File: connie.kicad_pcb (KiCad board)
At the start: 4 copper layers, 105.6 x 58 mm, 143 parts, among them J1 Conn_01x03, J2 Conn_01x02, J3 Conn_01x02, J4 Conn_01x03, J5 Barrel_Jack_Switch, Q1 DTC143Z, Q2 DTC143Z, Q3 DTC143Z, Q4 DTC143Z, SW1 DIP_1188E, SW2 DIP_1188E, SW3 DIP_1188E, SW4 DIP_1188E, SW5 DIP_1188E, U1 emmc_bga153, U2 ESP32_WROVER, U3 ES8388, U4 CS8676E, U5 74LVC1G02, U6 MAX803, U7 MAX803, U8 74LVC1G02, U9 TPS562200

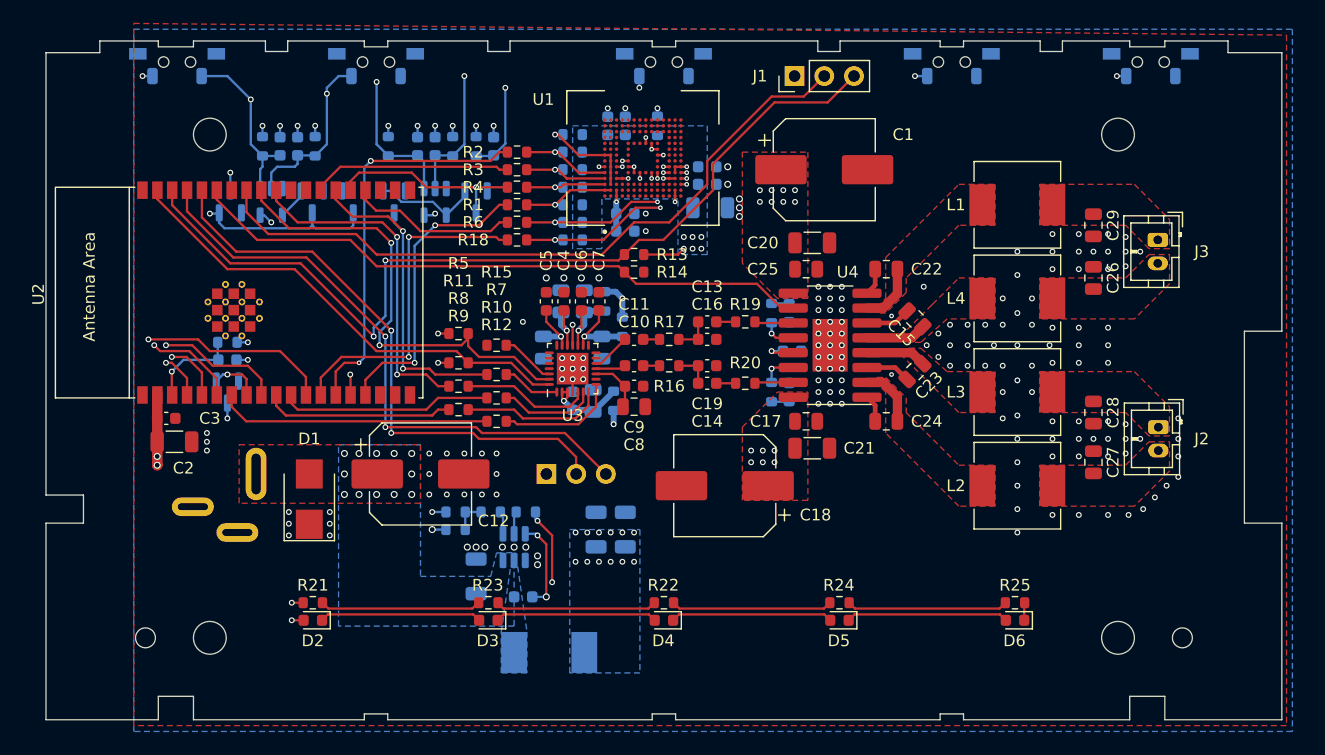
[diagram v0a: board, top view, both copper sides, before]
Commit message: add c3 module
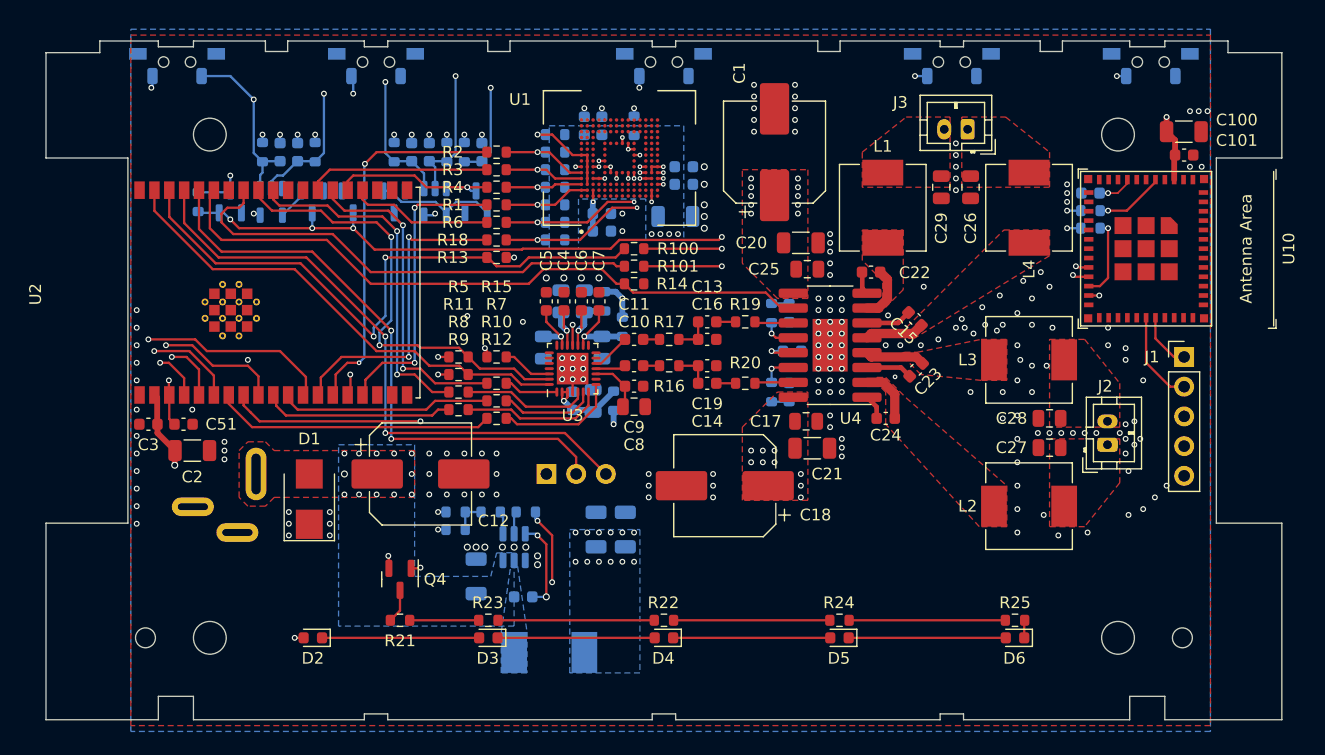
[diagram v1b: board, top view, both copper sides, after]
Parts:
- added C100: 22u, Capacitor_SMD:C_1206_3216Metric, F.Cu at (232.2, 31.8)
- added C101: 0.1u, Capacitor_SMD:C_0603_1608Metric, F.Cu at (232.2, 33.8)
- added C102: 0.1u, Capacitor_SMD:C_0603_1608Metric, B.Cu at (224.2, 37.0)
- added R100: 1k, Resistor_SMD:R_0603_1608Metric, F.Cu at (185.2, 41.8)
- added R101: 1k, Resistor_SMD:R_0603_1608Metric, F.Cu at (185.2, 43.2)
- added R103: 10k, Resistor_SMD:R_0603_1608Metric, B.Cu at (224.2, 38.5)
- added R104: 10k, Resistor_SMD:R_0603_1608Metric, B.Cu at (224.2, 40.0)
- added U10: ESP32-C3-mini-1, Espressif:ESP32-C3-MINI-1, F.Cu at (229.0, 41.8)
- C15, C22, C23, C24: footprint Capacitor_SMD:C_0805_2012Metric -> Capacitor_SMD:C_0603_1608Metric
- C51, Q4: moved to F.Cu
- J1: value Conn_01x03 -> Conn_01x05; footprint Connector_PinHeader_2.54mm:PinHeader_1x03_P2.54mm_Vertical -> Connector_PinHeader_2.54mm:PinHeader_1x05_P2.54mm_Vertical
- R26, R27, R28, R31, R32, R33, R42, R43: value R -> 10k
- moved J1 41.0 mm to (232.2, 51.0), turned to 0 degrees
- moved Q4 21.8 mm to (165.2, 70.0)
- moved J3 18.8 mm to (213.8, 31.6), turned to 180 degrees
- moved C29 13.4 mm to (211.5, 36.5)
- moved C26 13.1 mm to (214.0, 36.5), turned to 90 degrees
- moved R44 12.3 mm to (148.0, 37.8), turned to -90 degrees
- moved R13 11.8 mm to (173.5, 42.5)
- moved L1 11.5 mm to (206.5, 38.2), turned to -90 degrees
- moved L4 7.81 mm to (219.0, 38.2), turned to -90 degrees
- moved R21 7.60 mm to (165.2, 73.5)
- moved C51 6.66 mm to (146.8, 56.8)
- moved J2 4.60 mm to (225.7, 58.5), turned to 90 degrees
- moved C1 4.51 mm to (197.2, 33.5), turned to 90 degrees
- moved C27 3.95 mm to (220.8, 58.8), turned to 0 degrees
- moved C28 3.78 mm to (220.8, 56.2), turned to 180 degrees
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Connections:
- C37 pad 1: /MODE -> GND
- C37 pad 2: GND -> /MODE
- J1 pad 1: GND -> /C3_TXD0
- J1 pad 2: /RXD1 -> /C3_RXD0
- J1 pad 3: /TXD1 -> GND
- J2 pad 1: /OUTNR2 -> /OUTPR2
- J2 pad 2: /OUTPR2 -> /OUTNR2
- J3 pad 1: /OUTPL2 -> /OUTNL2
- J3 pad 2: /OUTNL2 -> /OUTPL2
- R35 pad 1: +3V3 -> /PLAY
- R35 pad 2: /PLAY -> +3V3
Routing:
- net /EN: track 38.3 -> 118.2 mm, vias 2 -> 6
- net /C3_TXD1: track 0.00 -> 50.9 mm, vias 0 -> 2
- net /C3_RXD1: track 0.00 -> 49.9 mm, vias 0 -> 2
- net /LED: track 4.09 -> 29.9 mm, vias 1 -> 2
- net /TXD1: track 77.7 -> 52.4 mm
- net Net-(J1-Pad5): track 0.00 -> 21.9 mm, vias 0 -> 1
- net Net-(Q4-Pad3): track 23.0 -> 2.90 mm, vias 2 -> 0
- net /RXD1: track 60.0 -> 40.7 mm
- net /C3_RXD0: track 0.00 -> 7.94 mm
- net Net-(R21-Pad1): track 13.7 -> 5.90 mm
- net Net-(R104-Pad2): track 0.00 -> 6.86 mm, vias 0 -> 1
- net Net-(R103-Pad2): track 0.00 -> 5.94 mm, vias 0 -> 1
- net /C3_TXD0: track 0.00 -> 4.88 mm
- net +3V3: track 32.5 -> 36.1 mm
- net /PA: track 53.7 -> 57.1 mm
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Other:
- outline, holes or cut-outs redrawn

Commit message: prepare to rename refs
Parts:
- renumbered R2 to R1, R3 to R2, R4 to R3, R1 to R4
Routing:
- net /PA: track 57.1 -> 56.2 mm

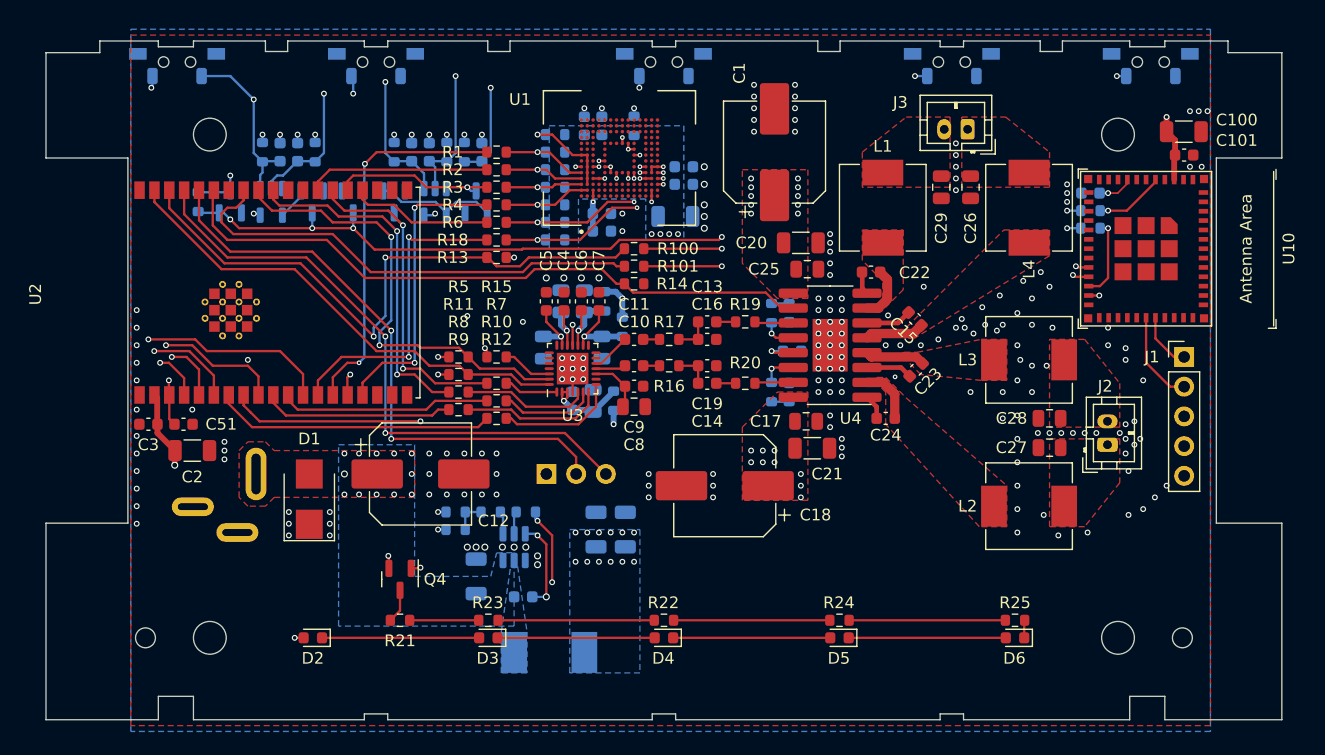
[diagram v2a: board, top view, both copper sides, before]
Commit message: reannotate resistors
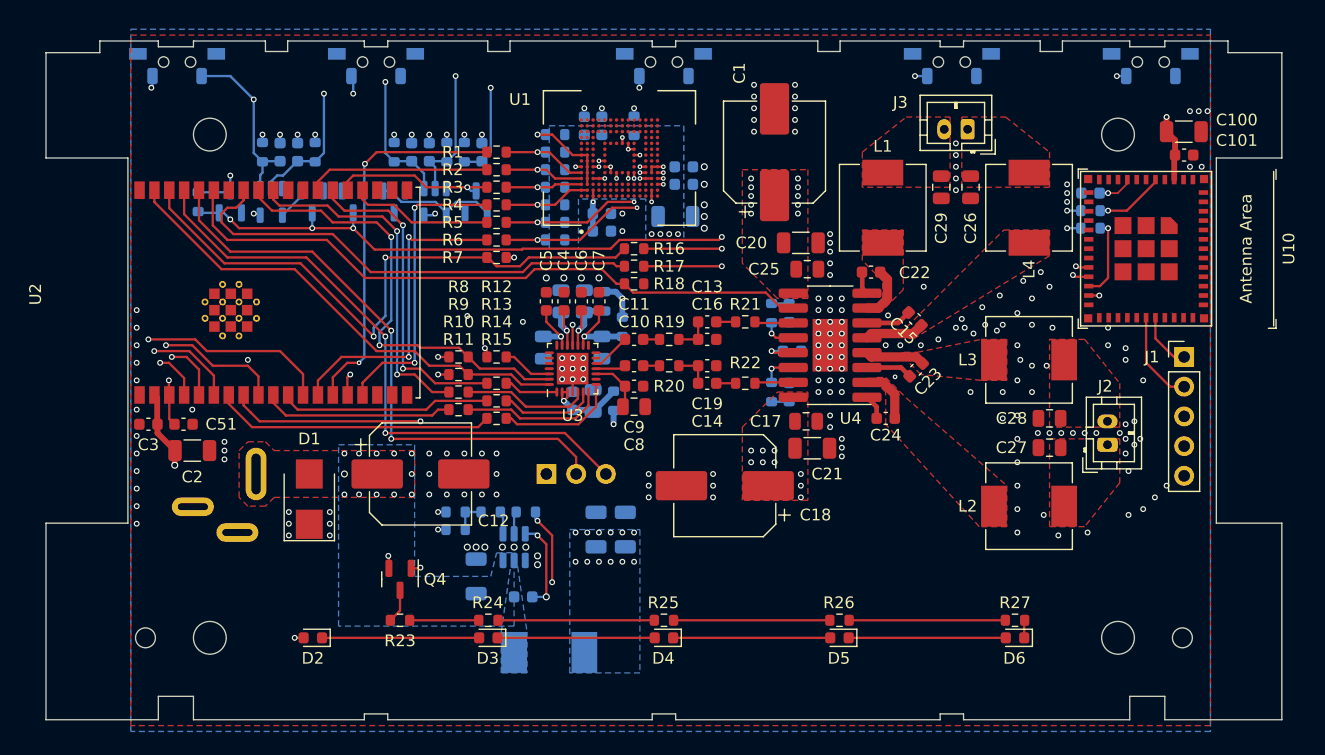
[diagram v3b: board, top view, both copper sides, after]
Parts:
- renumbered R8 to R10, R9 to R11, R15 to R12, R7 to R13, R10 to R14, R12 to R15, R100 to R16, R101 to R17, R14 to R18, R17 to R19, R16 to R20, R19 to R21, R20 to R22, R21 to R23, R23 to R24, R22 to R25, R24 to R26, R25 to R27, R103 to R28, R104 to R29, R28 to R30, R33 to R32, R27 to R33, R26 to R34, R32 to R35, R43 to R36, R42 to R37, R34 to R38, R35 to R39, R36 to R40, R30 to R41, R29 to R42, R44 to R43, R37 to R44, R38 to R45, R40 to R46, R39 to R47, R41 to R48, R48 to R49, R6 to R5, R45 to R50, R46 to R51, R47 to R52, R18 to R6, R13 to R7, R5 to R8, R11 to R9

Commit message: reannotate caps
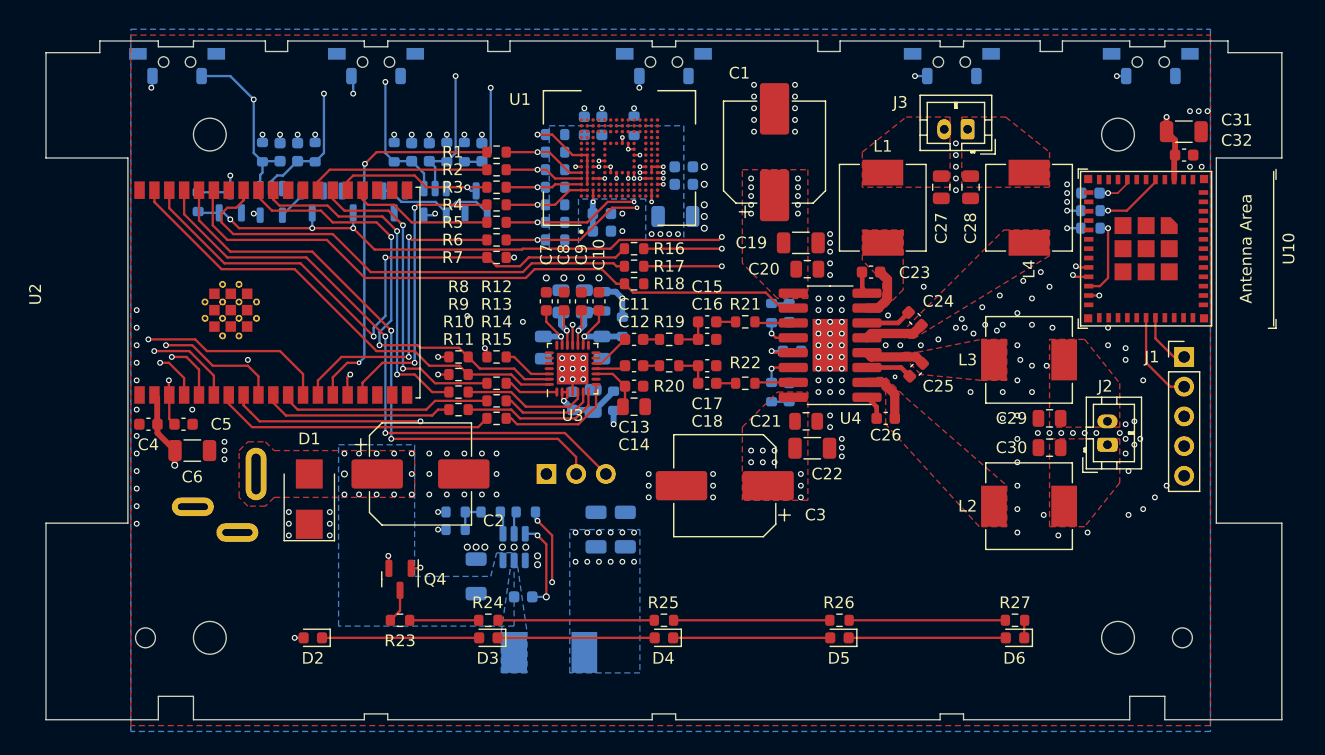
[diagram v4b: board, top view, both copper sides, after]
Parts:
- renumbered C7 to C10, C10 to C12, C9 to C13, C8 to C14, C13 to C15, C19 to C17, C14 to C18, C20 to C19, C12 to C2, C25 to C20, C17 to C21, C21 to C22, C22 to C23, C15 to C24, C23 to C25, C24 to C26, C29 to C27, C26 to C28, C28 to C29, C18 to C3, C27 to C30, C100 to C31, C101 to C32, C102 to C33, C30 to C34, C31 to C35, C40 to C36, C32 to C37, C33 to C38, C49 to C39, C3 to C4, C50 to C40, C37 to C41, C38 to C42, C35 to C43, C36 to C44, C34 to C45, C41 to C46, C39 to C47, C42 to C48, C46 to C49, C51 to C5, C48 to C50, C47 to C51, C43 to C52, C44 to C53, C45 to C54, C52 to C55, C53 to C56, C54 to C57, C55 to C58, C2 to C6, C5 to C7, C4 to C8, C6 to C9

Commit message: prepare for manufacturing
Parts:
- removed the U10 at (229.0, 41.8)
- added FID1: Fiducial, Fiducial:Fiducial_1mm_Mask2mm, F.Cu at (221.5, 75.0)
- added FID2: Fiducial, Fiducial:Fiducial_1mm_Mask2mm, F.Cu at (221.5, 32.0)
- added FID3: Fiducial, Fiducial:Fiducial_1mm_Mask2mm, F.Cu at (154.0, 75.0)
- added FID4: Fiducial, Fiducial:Fiducial_1mm_Mask2mm, B.Cu at (221.5, 32.0)
- added FID5: Fiducial, Fiducial:Fiducial_1mm_Mask2mm, B.Cu at (221.5, 75.0)
- added FID6: Fiducial, Fiducial:Fiducial_1mm_Mask2mm, B.Cu at (154.0, 75.0)
- added TP1: TestPoint, TestPoint:TestPoint_Pad_D1.0mm, B.Cu at (156.0, 43.0)
- added TP10: TestPoint, TestPoint:TestPoint_Pad_D1.5mm, B.Cu at (209.8, 31.6)
- added TP11: TestPoint, TestPoint:TestPoint_Pad_D1.5mm, B.Cu at (215.8, 31.6)
- added TP12: TestPoint, TestPoint:TestPoint_Pad_D1.5mm, B.Cu at (225.7, 60.5)
- added TP13: TestPoint, TestPoint:TestPoint_Pad_D1.5mm, B.Cu at (225.7, 54.5)
- added TP2: TestPoint, TestPoint:TestPoint_Pad_D1.0mm, B.Cu at (158.5, 43.0)
- added TP3: TestPoint, TestPoint:TestPoint_Pad_D1.0mm, B.Cu at (161.0, 43.0)
- added TP4: TestPoint, TestPoint:TestPoint_Pad_D1.0mm, B.Cu at (160.0, 33.5)
- added TP5: TestPoint, TestPoint:TestPoint_Pad_D1.0mm, B.Cu at (160.0, 31.0)
- added TP6: TestPoint, TestPoint:TestPoint_Pad_D1.0mm, B.Cu at (162.5, 31.0)
- added TP7: TestPoint, TestPoint:TestPoint_Pad_D1.0mm, B.Cu at (162.5, 33.5)
- added U5: ESP32-C3-MINI-1, Espressif:ESP32-C3-MINI-1, F.Cu at (229.0, 41.8)
- C1, C2, C3: value 220u -> 220u,35V
- C14, C49, C50, C51, C52, C54: value 10u -> 10u,0805
- C19, C22, C31, C36, C55, C57, C58, C6: value 22u -> 22u,1206,50V
- C20, C21: value 0.1u -> 0.1u,0805,50V
- C23, C24, C25, C26, C56: value 1u -> 1u,50V
- C27, C28, C29, C30: value 0.47u -> 0.47u,0805,50V
- C47: value 1u, 0603, 16V -> 1u,50V
- D1: value SMBJ15CA -> SMBJ15CA
- R16, R17: value 1k -> 33
- R19, R20, R21, R22, R44, R45: value 10 -> 100,1%
- R23, R24, R25, R26, R27: value 100 -> 100,1%
- R51: value 40.2k -> 40.2k,1%
- R52: value 13k -> 13k,1%
- U1: renamed from U2; value ESP32_WROVER -> ESP32-WROVER-E
- U2: renamed from U1; value emmc_bga153 -> EMMC(BGA153)
- moved R23 7.45 mm to (157.8, 73.5)
- moved Q1 3.50 mm to (165.2, 73.5)
- turned C43 to -90 degrees
- turned R49 to 0 degrees
- renumbered J3 to J1, J1 to J3, L4 to L2, L2 to L4, Q4 to Q1, Q1 to Q2, Q2 to Q3, Q3 to Q4, SW5 to SW1, SW4 to SW2, SW2 to SW4, SW1 to SW5, U9 to U10, U5 to U6, U6 to U9
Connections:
- C43 pad 1: /VOL- -> GND
- C43 pad 2: GND -> /VOL-
- D2 pad 2: +15V -> Net-(D2-Pad2)
- J3 pad 5: Net-(J1-Pad5) -> /C3_IO9
- Q1 pad 3: Net-(Q4-Pad3) -> Net-(Q1-Pad3)
- R23 pad 1: Net-(R23-Pad1) -> +15V
- R23 pad 2: Net-(Q4-Pad3) -> Net-(D2-Pad2)
- R24 pad 2: Net-(R23-Pad1) -> Net-(Q1-Pad3)
- R49 pad 1: +15V -> Net-(R49-Pad1)
- R49 pad 2: Net-(R49-Pad2) -> +15V
- U1 pad 17: unconnected-(U2-Pad17) -> (no net)
- U1 pad 18: unconnected-(U2-Pad18) -> (no net)
- U1 pad 19: unconnected-(U2-Pad19) -> (no net)
- U1 pad 20: unconnected-(U2-Pad20) -> (no net)
- U1 pad 21: unconnected-(U2-Pad21) -> (no net)
- U1 pad 22: unconnected-(U2-Pad22) -> (no net)
- U1 pad 27: unconnected-(U2-Pad27) -> (no net)
- U1 pad 28: unconnected-(U2-Pad28) -> (no net)
- U1 pad 32: unconnected-(U2-Pad32) -> (no net)
- U10 pad 5: Net-(R49-Pad2) -> Net-(R49-Pad1)
- U6 pad 1: /VOL- -> /MODE
- U6 pad 2: /VOL+ -> /PLAY
- U8 pad 1: /MODE -> /POWER
- U8 pad 2: /PLAY -> /MODE
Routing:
- net Net-(J1-Pad5): track 21.9 -> 0.00 mm, vias 1 -> 0
- net /C3_IO9: track 0.00 -> 21.9 mm, vias 0 -> 1
- net /MODE: track 47.7 -> 67.0 mm, vias 2 -> 4
- net /PLAY: track 59.7 -> 75.7 mm, vias 3 -> 4
- net /POWER: track 76.3 -> 85.3 mm, vias 3 -> 4
- net Net-(Q1-Pad3): track 0.00 -> 7.11 mm
- net Net-(R23-Pad1): track 5.90 -> 0.00 mm
- net /D0: track 14.2 -> 19.3 mm, vias 1 -> 2
- net /MCLK: track 29.0 -> 32.5 mm, vias 2 -> 3
- net /LED: track 29.9 -> 33.0 mm
- net Net-(Q4-Pad3): track 2.90 -> 0.00 mm
- net /VOL+: track 132.9 -> 130.0 mm
- net /VOL-: track 107.0 -> 104.3 mm
- net /OUTPR2: track 0.00 -> 2.00 mm, vias 0 -> 1
- net /OUTPL2: track 0.00 -> 2.00 mm, vias 0 -> 1
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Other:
- board text added: "B"
- board text added: "G"
- board text added: "RX"
- board text added: "TX"
